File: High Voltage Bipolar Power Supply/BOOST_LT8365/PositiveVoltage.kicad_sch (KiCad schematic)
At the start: 42 parts, among them J1 FCR7350R, J2 FCR7350B, Q1 FZT857, Q2 FZT857, U1 LT8365, U2 LM317_SOT-223, U5 LM329BZ

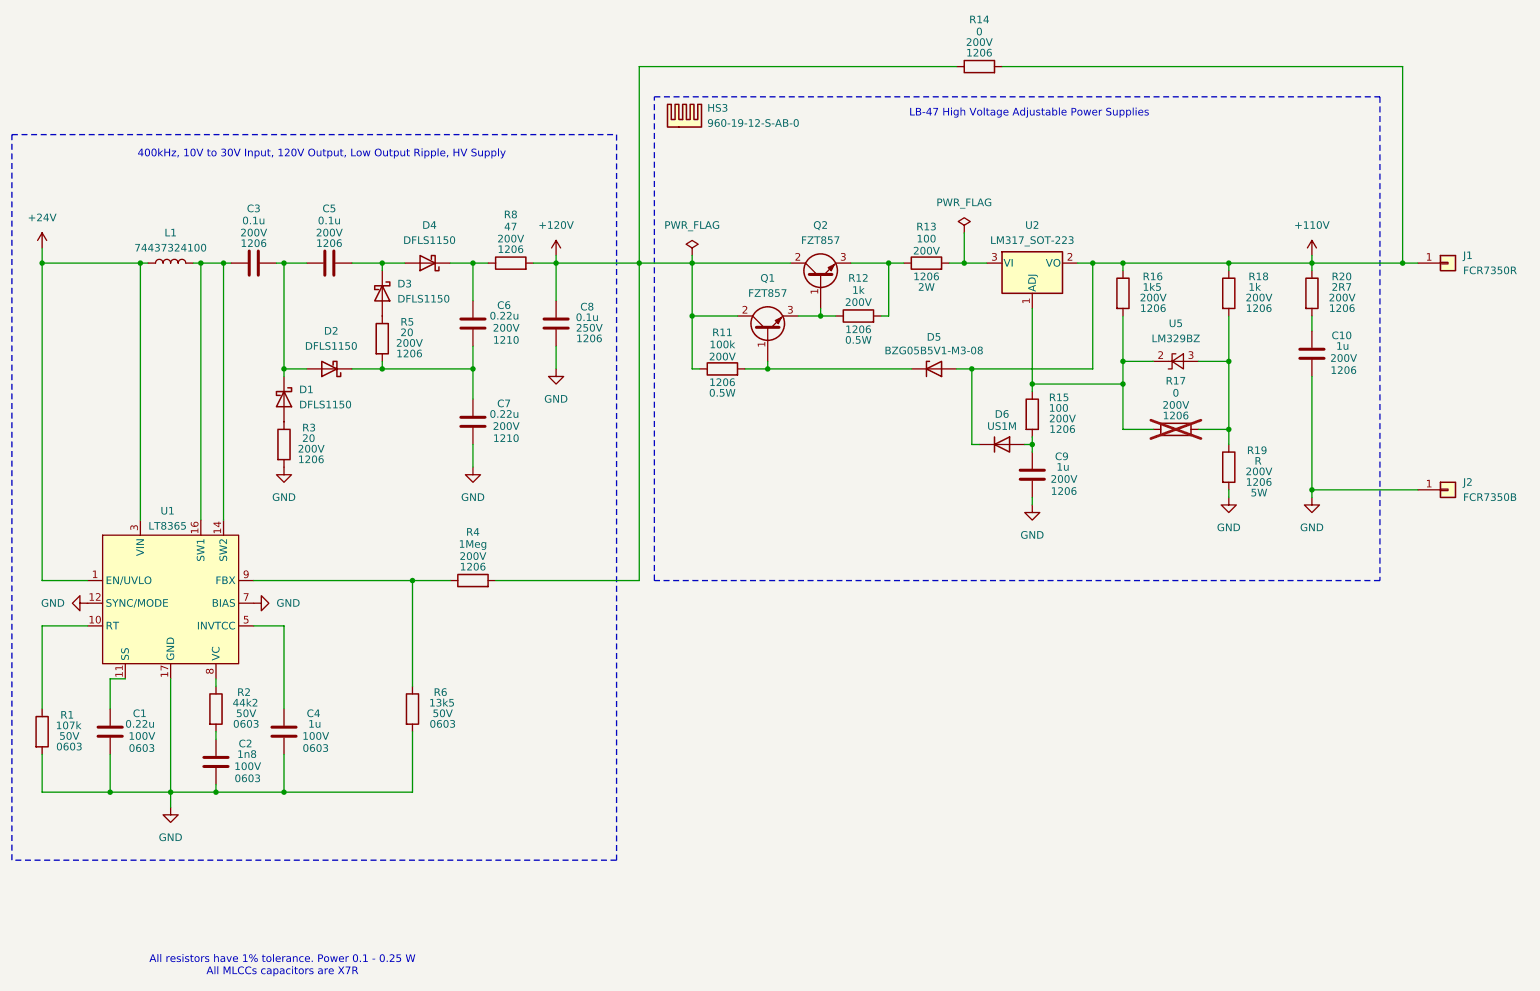
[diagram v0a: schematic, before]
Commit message: Deleted LM317 and LM337 regulator circuits because of current lost on the volateges setup resistors.
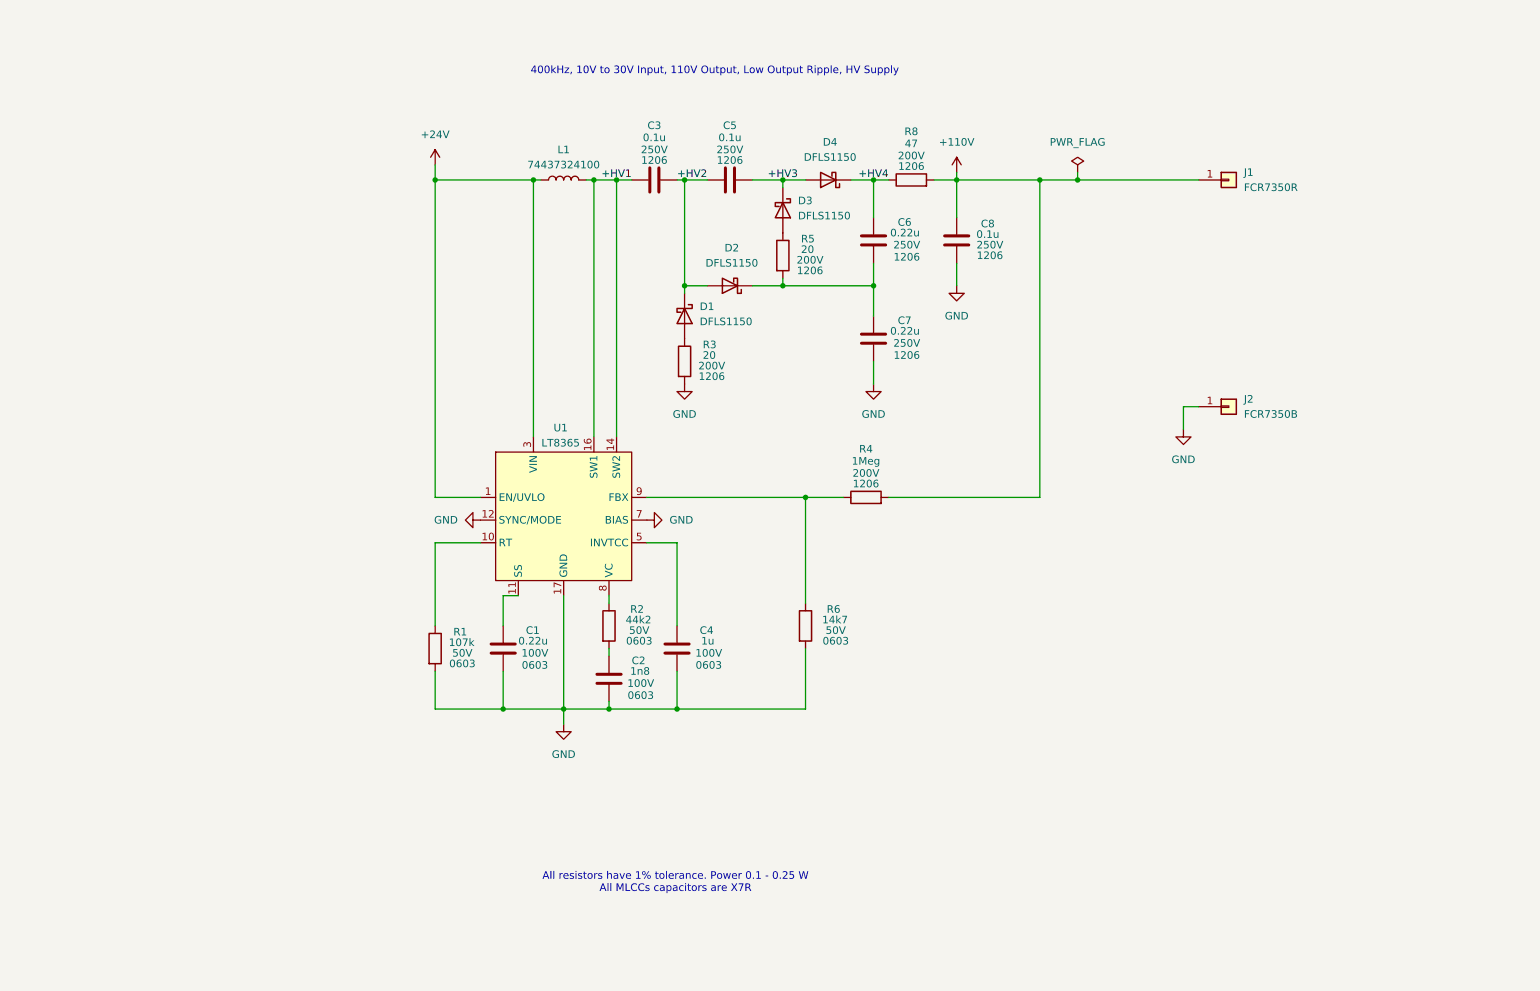
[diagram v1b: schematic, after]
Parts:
- removed C10, C9: 1u, symbol Device:C
- removed D5: BZG05B5V1-M3-08, symbol Device:D_Zener
- removed D6: US1M, Diode_SMD:D_SMA, symbol Diode:US1M
- removed HS3: 960-19-12-S-AB-0, BOOST_LT8365:960-19-12-S-AB-0, symbol Mechanical:Heatsink
- removed Q1, Q2: FZT857, Package_TO_SOT_SMD:SOT-223-3_TabPin2, symbol Device:Q_NPN_BCE
- removed R11: 100k, symbol Device:R
- removed R12, R18: 1k, symbol Device:R
- removed R13, R15: 100, symbol Device:R
- removed R14, R17: 0, symbol Device:R
- removed R16: 1k5, symbol Device:R
- removed R19: R, symbol Device:R
- removed R20: 2R7, symbol Device:R
- removed U2: LM317_SOT-223, Package_TO_SOT_SMD:SOT-223-3_TabPin2, symbol Regulator_Linear:LM317_SOT-223
- removed U5: LM329BZ, Package_TO_SOT_THT:TO-92_Inline_Horizontal2, symbol Reference_Voltage:LM329xZ
- C1, C2, C4: footprint (none) -> Capacitor_SMD:C_0603_1608Metric_Pad1.08x0.95mm_HandSolder
- C3, C5: footprint (none) -> Capacitor_SMD:C_1206_3216Metric_Pad1.33x1.80mm_HandSolder; Voltage 200V -> 250V
- C6, C7: footprint (none) -> Capacitor_SMD:C_1206_3216Metric_Pad1.33x1.80mm_HandSolder; Package 1210 -> 1206; Voltage 200V -> 250V
- C8: footprint (none) -> Capacitor_SMD:C_1206_3216Metric_Pad1.33x1.80mm_HandSolder
- D1, D2, D3, D4: footprint (none) -> Diode_SMD:D_PowerDI-123
- R1, R2: footprint (none) -> Resistor_SMD:R_0603_1608Metric_Pad0.98x0.95mm_HandSolder
- R3, R4, R5, R8: footprint (none) -> Resistor_SMD:R_1206_3216Metric_Pad1.30x1.75mm_HandSolder
- R6: value 13k5 -> 14k7; footprint (none) -> Resistor_SMD:R_0603_1608Metric_Pad0.98x0.95mm_HandSolder
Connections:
- net +120V is gone; now on net +110V: C8.1, R4.2, R8.2
- net +HV2: now reaches C3.2, C5.1, D1.1 (K), D2.2 (A)
- net +HV3: now reaches C5.2, D3.1 (K), D4.2 (A)
- net +HV1: now reaches C3.1, L1.2, U1.14 (SW2), U1.16 (SW1)
- net +HV4: now reaches C6.1, D4.1 (K), R8.1
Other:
- note added: "400kHz, 10V to 30V Input, 110V Output, Low Output Ripple, HV Supply"
- note removed: "400kHz, 10V to 30V Input, 120V Output, Low Output Ripple, HV Supply"
- note removed: "LB-47 High Voltage Adjustable Power Supplies"
- moved on the sheet: C1, C2, C3, C4, C5, C6, C7, C8, D1, D2, D3, D4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

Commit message: BOOST_LT8365 : PCB layout
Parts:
- J1, J2: footprint (none) -> BOOST_LT8365:S16N-PC
- L1: footprint (none) -> BOOST_LT8365:74437324100
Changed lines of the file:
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@@
 			)
 		)
-		(property "Footprint" ""
+		(property "Footprint" "BOOST_LT8365:S16N-PC"
 			(at 229.87 50.8 0)
 			(effects
@@
 			)
 		)
-		(property "Footprint" ""
+		(property "Footprint" "BOOST_LT8365:74437324100"
 			(at 118.11 50.8 0)
 			(effects
@@
 			)
 		)
-		(property "Footprint" ""
+		(property "Footprint" "BOOST_LT8365:S16N-PC"
 			(at 229.87 88.9 0)
 			(effects

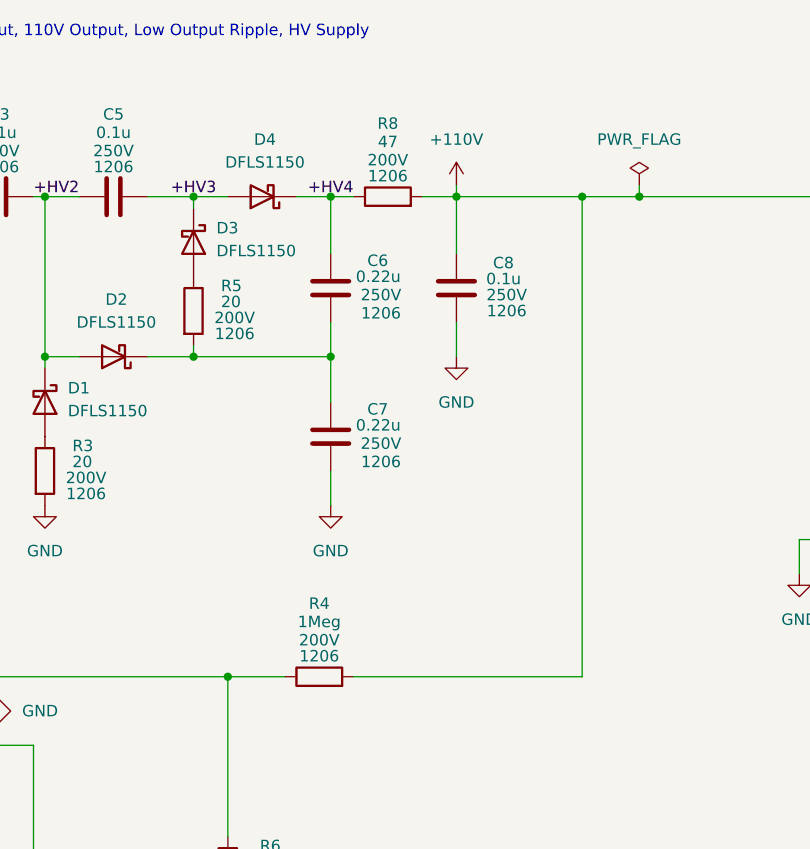
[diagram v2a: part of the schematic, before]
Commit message: BOOST_LT8365 : PCB design done
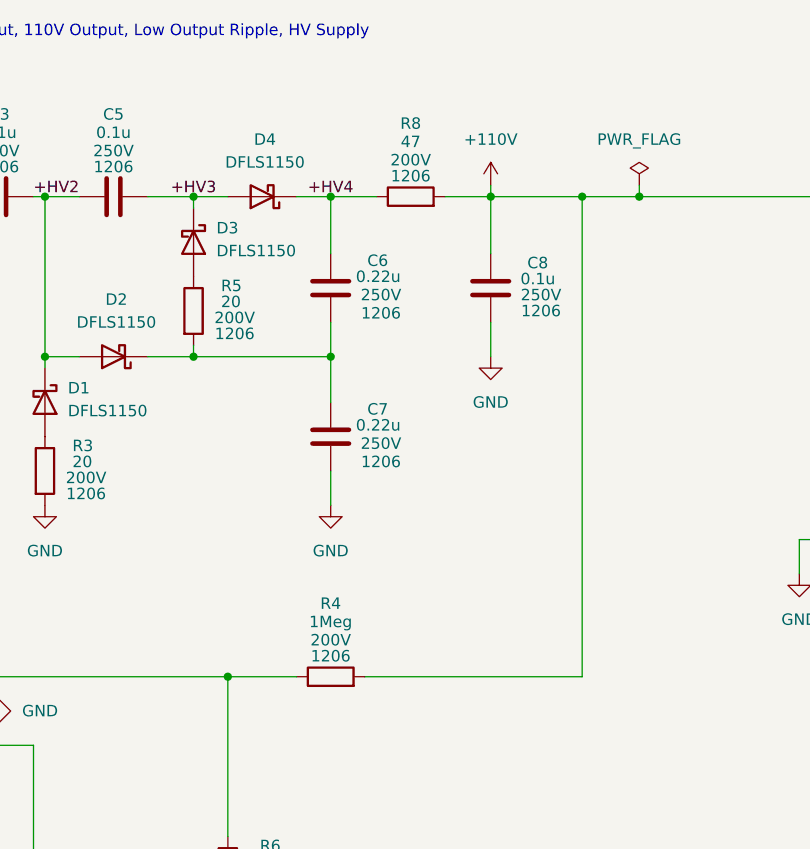
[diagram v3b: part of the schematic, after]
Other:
- moved on the sheet: C8, R4, R8
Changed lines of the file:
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@@
 	)
 	(junction
-		(at 184.15 50.8)
+		(at 187.96 50.8)
 		(diameter 0)
 		(color 0 0 0 0)
@@
 	(wire
 		(pts
-			(xy 184.15 50.8) (xy 180.34 50.8)
-		)
-		(stroke
-			(width 0)
-			(type default)
-		)
-	)
-	(wire
-		(pts
 			(xy 149.86 50.8) (xy 154.94 50.8)
 		)
@@
 	(wire
 		(pts
-			(xy 172.72 104.14) (xy 198.12 104.14)
+			(xy 173.99 104.14) (xy 198.12 104.14)
 		)
 		(stroke
@@
 	(wire
 		(pts
+			(xy 198.12 50.8) (xy 204.47 50.8)
+		)
+		(stroke
+			(width 0)
+			(type default)
+		)
+	)
+	(wire
+		(pts
 			(xy 170.18 50.8) (xy 166.37 50.8)
 		)
@@
 	(wire
 		(pts
-			(xy 158.75 104.14) (xy 165.1 104.14)
+			(xy 158.75 104.14) (xy 166.37 104.14)
 		)
 		(stroke
@@
 	(wire
 		(pts
-			(xy 184.15 50.8) (xy 198.12 50.8)
+			(xy 187.96 50.8) (xy 198.12 50.8)
 		)
 		(stroke
@@
 	(wire
 		(pts
-			(xy 198.12 50.8) (xy 204.47 50.8)
-		)
-		(stroke
-			(width 0)
-			(type default)
-		)
-	)
-	(wire
-		(pts
 			(xy 204.47 50.8) (xy 224.79 50.8)
 		)
@@
 	(wire
 		(pts
+			(xy 182.88 50.8) (xy 187.96 50.8)
+		)
+		(stroke
+			(width 0)
+			(type default)
+		)
+	)
+	(wire
+		(pts
 			(xy 154.94 50.8) (xy 154.94 52.07)
 		)
@@
 	(wire
 		(pts
-			(xy 170.18 50.8) (xy 172.72 50.8)
+			(xy 170.18 50.8) (xy 175.26 50.8)
 		)
 		(stroke
@@
 	(wire
 		(pts
-			(xy 184.15 49.53) (xy 184.15 50.8)
+			(xy 187.96 49.53) (xy 187.96 50.8)
 		)
 		(stroke
@@
 	(wire
 		(pts
-			(xy 184.15 57.15) (xy 184.15 50.8)
+			(xy 187.96 57.15) (xy 187.96 50.8)
 		)
 		(stroke
@@
 	(wire
 		(pts
-			(xy 184.15 64.77) (xy 184.15 68.58)
+			(xy 187.96 64.77) (xy 187.96 68.58)
 		)
 		(stroke
@@
 	(symbol
 		(lib_id "Device:R")
-		(at 168.91 104.14 90)
+		(at 170.18 104.14 90)
 		(unit 1)
 		(exclude_from_sim no)
@@
 		(dnp no)
 		(property "Reference" "R4"
-			(at 168.91 96.012 90)
+			(at 170.18 96.012 90)
 			(effects
 				(font
@@
 		)
 		(property "Value" "1Meg"
-			(at 168.91 98.044 90)
+			(at 170.18 98.044 90)
 			(effects
 				(font
@@
 		)
 		(property "Footprint" "Resistor_SMD:R_1206_3216Metric_Pad1.30x1.75mm_HandSolder"
-			(at 168.91 105.918 90)
+			(at 170.18 105.918 90)
 			(effects
 				(font
@@
 		)
 		(property "Datasheet" "~"
-			(at 168.91 104.14 0)
+			(at 170.18 104.14 0)
 			(effects
 				(font
@@
 		)
 		(property "Description" "Resistor"
-			(at 168.91 104.14 0)
+			(at 170.18 104.14 0)
 			(effects
 				(font
@@
 		)
 		(property "Voltage" "200V"
-			(at 168.91 100.076 90)
+			(at 170.18 100.076 90)
 			(effects
 				(font
@@
 		)
 		(property "Package" "1206"
-			(at 168.91 101.854 90)
+			(at 170.18 101.854 90)
 			(effects
 				(font
@@
 	(symbol
 		(lib_id "Device:R")
-		(at 176.53 50.8 90)
+		(at 179.07 50.8 90)
 		(unit 1)
 		(exclude_from_sim no)
@@
 		(dnp no)
 		(property "Reference" "R8"
-			(at 176.53 42.672 90)
+			(at 179.07 42.672 90)
 			(effects
 				(font
@@
 		)
 		(property "Value" "47"
-			(at 176.53 44.704 90)
+			(at 179.07 44.704 90)
 			(effects
 				(font
@@
 		)
 		(property "Footprint" "Resistor_SMD:R_1206_3216Metric_Pad1.30x1.75mm_HandSolder"
-			(at 176.53 52.578 90)
+			(at 179.07 52.578 90)
 			(effects
 				(font
@@
 		)
 		(property "Datasheet" "~"
-			(at 176.53 50.8 0)
+			(at 179.07 50.8 0)
 			(effects
 				(font
@@
 		)
 		(property "Description" "Resistor"
-			(at 176.53 50.8 0)
+			(at 179.07 50.8 0)
 			(effects
 				(font
@@
 		)
 		(property "Voltage" "200V"
-			(at 176.53 46.736 90)
+			(at 179.07 46.736 90)
 			(effects
 				(font
@@
 		)
 		(property "Package" "1206"
-			(at 176.53 48.514 90)
+			(at 179.07 48.514 90)
 			(effects
 				(font
@@
 	(symbol
 		(lib_id "Device:C")
-		(at 184.15 60.96 0)
+		(at 187.96 60.96 0)
 		(unit 1)
 		(exclude_from_sim no)
@@
 		(dnp no)
 		(property "Reference" "C8"
-			(at 188.214 58.166 0)
+			(at 192.024 58.166 0)
 			(effects
 				(font
@@
 		)
 		(property "Value" "0.1u"
-			(at 187.452 59.9439 0)
+			(at 191.262 59.9439 0)
 			(effects
 				(font
@@
 		)
 		(property "Footprint" "Capacitor_SMD:C_1206_3216Metric_Pad1.33x1.80mm_HandSolder"
-			(at 185.1152 64.77 0)
+			(at 188.9252 64.77 0)
 			(effects
 				(font
@@
 		)
 		(property "Datasheet" "~"
-			(at 184.15 60.96 0)
+			(at 187.96 60.96 0)
 			(effects
 				(font
@@
 		)
 		(property "Description" "Unpolarized capacitor"
-			(at 184.15 60.96 0)
+			(at 187.96 60.96 0)
 			(effects
 				(font
@@
 		)
 		(property "Voltage" "250V"
-			(at 189.738 61.722 0)
+			(at 193.548 61.722 0)
 			(effects
 				(font
@@
 		)
 		(property "Package" "1206"
-			(at 189.738 63.5 0)
+			(at 193.548 63.5 0)
 			(effects
 				(font
@@
 	(symbol
 		(lib_id "power:GND")
-		(at 184.15 68.58 0)
+		(at 187.96 68.58 0)
 		(unit 1)
 		(exclude_from_sim no)
@@
 		(fields_autoplaced yes)
 		(property "Reference" "#PWR07"
-			(at 184.15 74.93 0)
+			(at 187.96 74.93 0)
 			(effects
 				(font
@@
 		)
 		(property "Value" "GND"
-			(at 184.15 73.66 0)
+			(at 187.96 73.66 0)
 			(effects
 				(font
@@
 		)
 		(property "Footprint" ""
-			(at 184.15 68.58 0)
+			(at 187.96 68.58 0)
 			(effects
 				(font
@@
 		)
 		(property "Datasheet" ""
-			(at 184.15 68.58 0)
+			(at 187.96 68.58 0)
 			(effects
 				(font
@@
 		)
 		(property "Description" "Power symbol creates a global label with name \"GND\" , ground"
-			(at 184.15 68.58 0)
+			(at 187.96 68.58 0)
 			(effects
 				(font
@@
 	(symbol
 		(lib_id "BOOST_LT8365:+110V")
-		(at 184.15 49.53 0)
+		(at 187.96 49.53 0)
 		(unit 1)
 		(exclude_from_sim no)
@@
 		(fields_autoplaced yes)
 		(property "Reference" "#PWR09"
-			(at 184.15 53.34 0)
+			(at 187.96 53.34 0)
 			(effects
 				(font
@@
 		)
 		(property "Value" "+110V"
-			(at 184.15 44.45 0)
+			(at 187.96 44.45 0)
 			(effects
 				(font
@@
 		)
 		(property "Footprint" ""
-			(at 184.15 49.53 0)
+			(at 187.96 49.53 0)
 			(effects
 				(font
@@
 		)
 		(property "Datasheet" ""
-			(at 184.15 49.53 0)
+			(at 187.96 49.53 0)
 			(effects
 				(font
@@
 		)
 		(property "Description" "Power symbol creates a global label"
-			(at 184.15 49.53 0)
-			(effects
-				(font
+			(at 187.96 49.53 0)
+			(effects
+				(font
